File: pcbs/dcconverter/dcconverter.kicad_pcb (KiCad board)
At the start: 2 copper layers, 149.9 x 149.9 mm, 41 parts, among them IC1 NCP7805TG, J1 190-9991, J2 766-6629, J3 146-8335, J4 766-6604, J5 766-6604, Q1 NGTB40N120FL2WG, Q10 398-433, Q2 FQP47P06, Q3 2SK3747-1E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

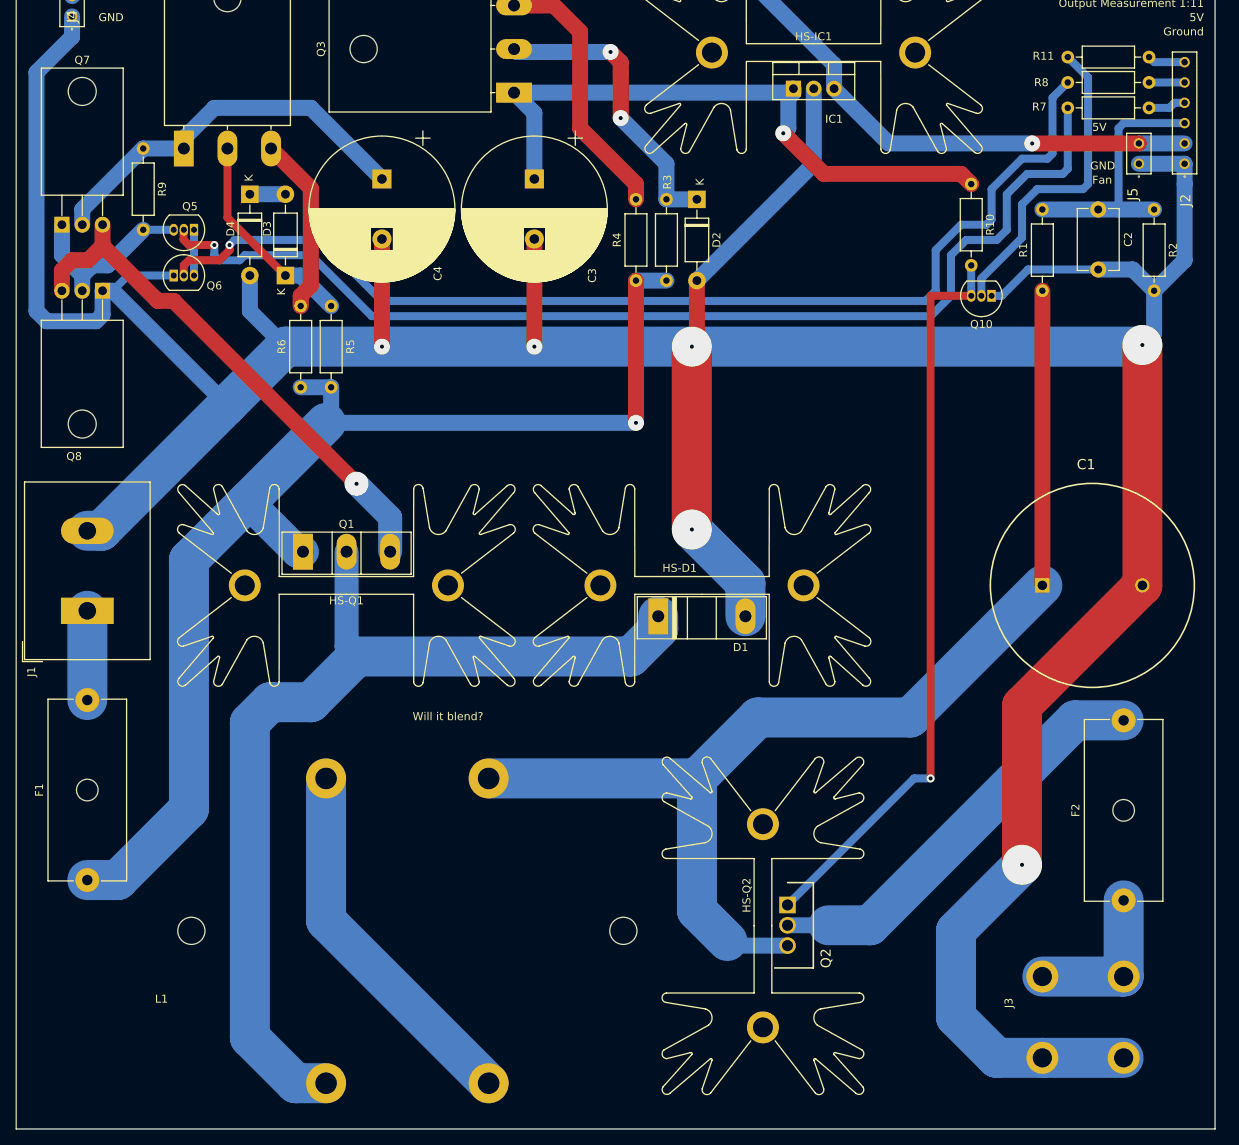
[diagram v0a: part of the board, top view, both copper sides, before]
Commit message: Make Tracks with a high Current as thick as possible
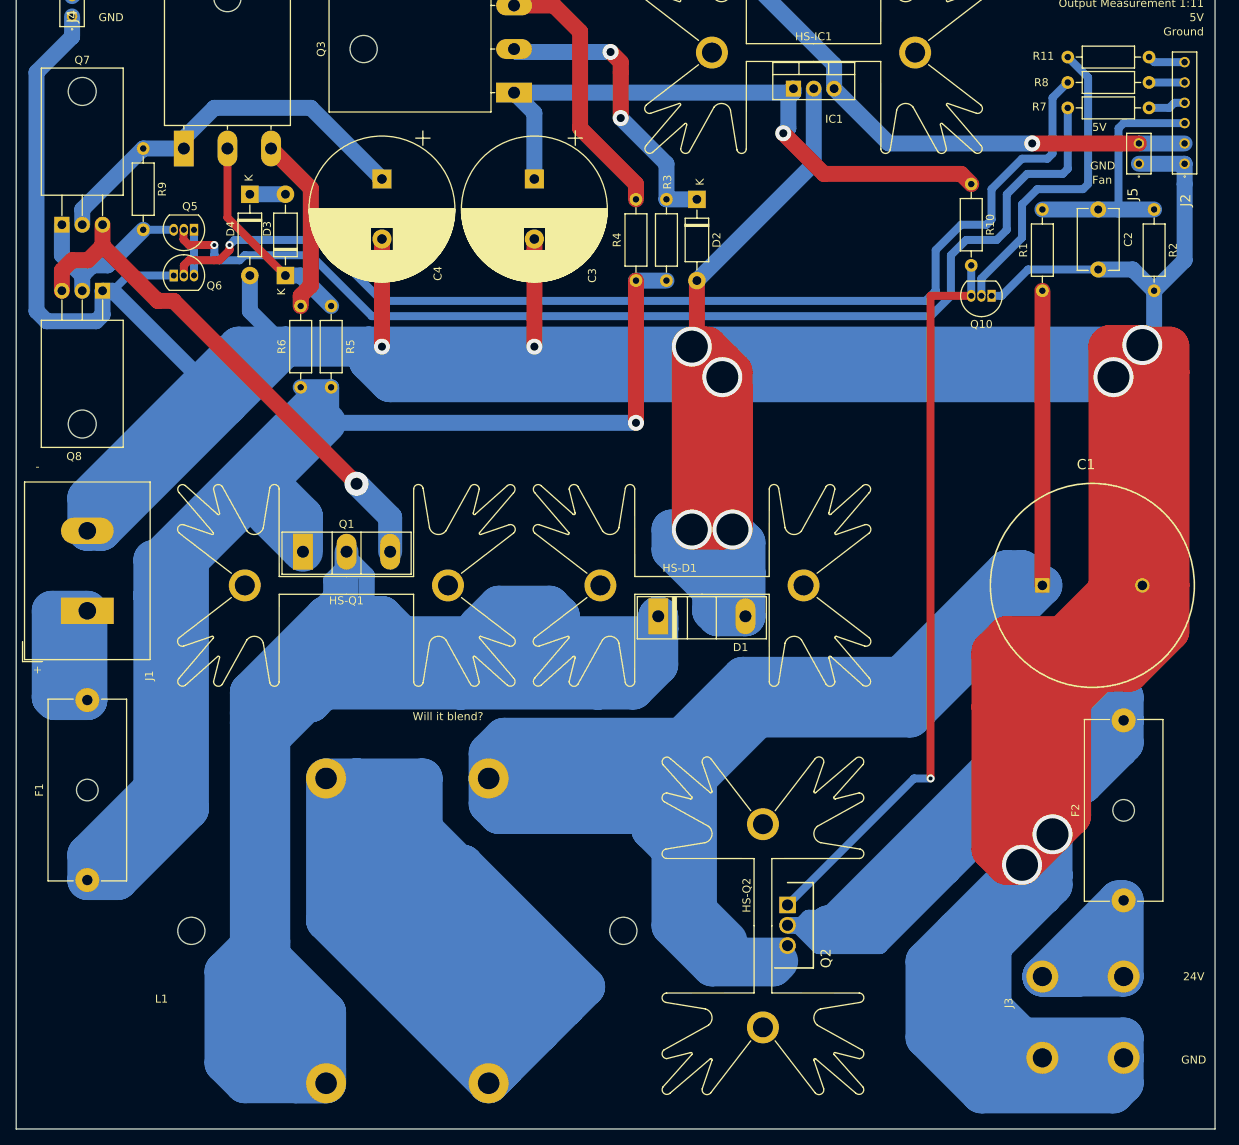
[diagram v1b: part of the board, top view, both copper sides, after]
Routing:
- net Net-(C1-Pad2): track 505.8 -> 1087.3 mm, vias 6 -> 10
- net Net-(D1-Pad1): track 122.4 -> 421.2 mm
- net Net-(C1-Pad1): track 145.7 -> 365.8 mm
- net Net-(L1-Pad2): track 46.5 -> 234.7 mm
- net Net-(F2-Pad2): track 52.6 -> 199.9 mm
- net Net-(F1-Pad1): track 149.8 -> 238.6 mm
- net Net-(F1-Pad2): track 11.2 -> 35.6 mm
- net Net-(F2-Pad1): track 19.7 -> 41.8 mm
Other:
- board text added: "+"
- board text added: "-"
- board text added: "24V"

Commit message: Empty PCB
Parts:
- removed C1: 845-4749, SamacSys_Parts:CAPPRD1250W100D2550H5200
- removed C2: 831-2929, Capacitor_THT:C_Disc_D7.5mm_W5.0mm_P7.50mm
- removed C3, C4: 711-2096, Capacitor_THT:CP_Radial_D18.0mm_P7.50mm
- removed D1: 192-966, Diode_THT:D_DO-247_Vertical
- removed D2: 805-0094, Diode_THT:D_DO-41_SOD81_P10.16mm_Horizontal
- removed D3, D4: 800-8872, Diode_THT:D_DO-41_SOD81_P10.16mm_Horizontal
- removed F1, F2: 176-9047, Fuse:Fuseholder_Cylinder-5x20mm_Schurter_0031_8201_Horizontal_Open
- removed HS-D1, HS-IC1, HS-Q1, HS-Q2: 893-4942, Heatsink:Heatsink_Fischer_SK129-STS_42x25mm_2xDrill2.5mm
- removed IC1: NCP7805TG, Package_TO_SOT_THT:TO-220-3_Vertical
- removed J1: 190-9991, TerminalBlock_Dinkle:TerminalBlock_Dinkle_DT-55-B01X-02_P10.00mm
- removed J2: 766-6629, SamacSys_Parts:CES-106-XX-Y-S
- removed J3: 146-8335, dcconverter:connector_2pin_P10.6mm
- removed J4, J5: 766-6604, SamacSys_Parts:CES-102-XX-Y-S
- removed L1: 769-0587, dcconverter:rb8522_size5
- removed Q1: NGTB40N120FL2WG, Package_TO_SOT_THT:TO-247-3_Vertical
- removed Q10, Q5, Q6: 398-433, Package_TO_SOT_THT:TO-92_Inline
- removed Q2: FQP47P06, TO254P483X1016X2261-3P
- removed Q3, Q4: 2SK3747-1E, Package_TO_SOT_THT:TO-3P-3_Horizontal_TabDown
- removed Q7: 671-5118, Package_TO_SOT_THT:TO-220-3_Horizontal_TabDown
- removed Q8: 671-4809, Package_TO_SOT_THT:TO-220-3_Horizontal_TabDown
- removed R1: 1M, Resistor_THT:R_Axial_DIN0207_L6.3mm_D2.5mm_P10.16mm_Horizontal
- removed R10: 10k, Resistor_THT:R_Axial_DIN0207_L6.3mm_D2.5mm_P10.16mm_Horizontal
- removed R11, R7, R8: 220, Resistor_THT:R_Axial_DIN0207_L6.3mm_D2.5mm_P10.16mm_Horizontal
- removed R2: 100k, Resistor_THT:R_Axial_DIN0207_L6.3mm_D2.5mm_P10.16mm_Horizontal
- removed R3, R5: 10M, Resistor_THT:R_Axial_DIN0207_L6.3mm_D2.5mm_P10.16mm_Horizontal
- removed R4, R6: 707-8546, Resistor_THT:R_Axial_DIN0207_L6.3mm_D2.5mm_P10.16mm_Horizontal
- removed R9: 1k, Resistor_THT:R_Axial_DIN0207_L6.3mm_D2.5mm_P10.16mm_Horizontal
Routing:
- net Net-(C1-Pad2): track 1087.3 -> 0.00 mm, vias 10 -> 0
- net Net-(D1-Pad1): track 421.2 -> 0.00 mm
- net Net-(C1-Pad1): track 365.8 -> 0.00 mm
- net Net-(F1-Pad1): track 238.6 -> 0.00 mm, vias 1 -> 0
- net Net-(L1-Pad2): track 234.7 -> 0.00 mm
- net Net-(F2-Pad2): track 199.9 -> 0.00 mm
- net Net-(IC1-Pad3): track 152.1 -> 0.00 mm, vias 1 -> 0
- net Net-(Q5-Pad2): track 137.8 -> 0.00 mm, vias 1 -> 0
- net Net-(Q6-Pad2): track 137.2 -> 0.00 mm, vias 1 -> 0
- net Net-(Q10-Pad3): track 93.7 -> 0.00 mm, vias 1 -> 0
- net Net-(C3-Pad1): track 79.2 -> 0.00 mm, vias 1 -> 0
- net Net-(Q1-Pad3): track 65.8 -> 0.00 mm, vias 1 -> 0
- net Net-(C4-Pad1): track 49.1 -> 0.00 mm
- net Net-(F2-Pad1): track 41.8 -> 0.00 mm
- net Net-(Q10-Pad2): track 39.8 -> 0.00 mm
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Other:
- board outline removed
- board text removed: "+"
- board text removed: "-"
- board text removed: "24V"
- board text removed: "5V"
- board text removed: "Controller Connection Pins"
- board text removed: "Fan"
- board text removed: "GND"
- board text removed: "Ground"
- board text removed: "IGBT Control Signal (5V)"
- board text removed: "IGBT ON/OFF (5V)"
- board text removed: "Output Measurement 1:11"
- board text removed: "Output ON/OFF (5V)"
- board text removed: "Will it blend?"

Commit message: Fix Heatsinks
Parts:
- added C1: 10mF, Custom:CAPPRD1250W100D2550H5200, F.Cu at (121.9, 115.6)
- added C2: 10nF, Capacitor_THT:C_Disc_D14.5mm_W5.0mm_P7.50mm, F.Cu at (174.3, 76.1)
- added C3: 1uF, Capacitor_THT:CP_Radial_D8.0mm_P2.50mm, F.Cu at (162.4, 118.7)
- added C4: 10nF, Capacitor_THT:C_Disc_D14.5mm_W5.0mm_P7.50mm, F.Cu at (157.3, 98.5)
- added C5: 1uF, Capacitor_THT:CP_Radial_D8.0mm_P2.50mm, F.Cu at (172.8, 104.4)
- added D1: DSS60-0045B, Custom:DSS60-0045B_Vertical, F.Cu at (110.8, 132.0)
- added D2: 1N4751ATR, Diode_THT:D_DO-41_SOD81_P10.16mm_Horizontal, F.Cu at (95.5, 104.3)
- added D3: 1N5956BRLG, Diode_THT:D_DO-41_SOD81_P10.16mm_Horizontal, F.Cu at (121.8, 83.6)
- added D4: 1N5956BRLG, Diode_THT:D_DO-41_SOD81_P10.16mm_Horizontal, F.Cu at (77.6, 133.4)
- added D5: 1N5408G, Custom:1N5408G, F.Cu at (104.1, 84.1)
- added F1: 2A, Fuse:Fuseholder_Cylinder-5x20mm_Schurter_0031_8201_Horizontal_Open, F.Cu at (181.4, 45.3)
- added F2: 25A, Fuse:Fuseholder_Cylinder-5x20mm_Schurter_0031_8201_Horizontal_Open, F.Cu at (82.8, 125.7)
- added HS-D1: HeatsinkUpright, Custom:HeatsinkUpright, F.Cu at (120.5, 47.3)
- added HS-IC1: HeatsinkUpright, Custom:HeatsinkUpright, F.Cu at (61.0, 114.3)
- added HS-Q1: HeatsinkUpright, Custom:HeatsinkUpright, F.Cu at (113.2, 94.7)
- added HS-Q2: HeatsinkUpright, Custom:HeatsinkUpright, F.Cu at (159.6, 47.3)
- added IC1: NCP7805TG, Package_TO_SOT_THT:TO-220-3_Vertical, F.Cu at (141.6, 132.8)
- added J1: 190-9991, Custom:TerminalBlock_2pin_10mm, F.Cu at (150.1, 115.2)
- added J2: Conn_01x01, Custom:SLB4-I90, F.Cu at (101.6, 67.4)
- added J3: Conn_01x01, Custom:SLB4-I90, F.Cu at (42.1, 134.5)
- added J4: 146-8335, Custom:connector_2pin_P10.6mm, F.Cu at (196.5, 68.0)
- added J5: Conn_01x01, Custom:SLB4-I90, F.Cu at (81.3, 119.3)
- added J6: Conn_01x01, Custom:SLB4-I90, F.Cu at (101.6, 80.7)
- added J7: 483-8461, Custom:Molex_KK_254_2pin, F.Cu at (206.9, 46.1)
- added J8: 483-8461, Custom:Molex_KK_254_2pin, F.Cu at (108.3, 126.5)
- added L1: RB8522-25-2M0, Custom:rb8522_size5, F.Cu at (71.1, 63.4)
- added Q1: NGTB40N120FL2WG, Custom:NGTB40N120FL2WG_Vertical, F.Cu at (156.3, 91.8)
- added Q10: TS13003CT, Custom:TS13003CT_wide, F.Cu at (171.5, 58.1)
- added Q2: FQP47P06, Custom:FQP47P06_Vertical_Wide, F.Cu at (195.6, 75.0)
- added Q3: 2SK3747-1E, Custom:2SK3747_TabDown, F.Cu at (155.8, 82.6)
- added Q4: 2SK3747-1E, Custom:2SK3747_TabDown, F.Cu at (138.4, 82.6)
- added Q5: TS13003CT, Custom:TS13003CT_wide, F.Cu at (171.5, 69.7)
- added Q6: TS13003CT, Custom:TS13003CT_wide, F.Cu at (171.5, 63.9)
- added Q7: FQP3P50, Custom:FQP3P50_Horizontal_TabDown, F.Cu at (144.8, 108.9)
- added Q8: FDP20N50, Custom:FDP20N50_Horizontal_TabDown, F.Cu at (182.4, 71.1)
- added R1: 1MOhm, Resistor_THT:R_Axial_DIN0207_L6.3mm_D2.5mm_P10.16mm_Horizontal, F.Cu at (171.6, 81.4)
- added R10: 10kOhm, Resistor_THT:R_Axial_DIN0207_L6.3mm_D2.5mm_P10.16mm_Horizontal, F.Cu at (184.9, 81.4)
- added R11: 220, Resistor_THT:R_Axial_DIN0207_L6.3mm_D2.5mm_P10.16mm_Horizontal, F.Cu at (160.2, 111.9)
- added R12: 10kOhm, Resistor_THT:R_Axial_DIN0207_L6.3mm_D2.5mm_P10.16mm_Horizontal, F.Cu at (184.9, 85.5)
- added R13: 10MOhm, Resistor_THT:R_Axial_DIN0207_L6.3mm_D2.5mm_P10.16mm_Horizontal, F.Cu at (91.2, 133.3)
- added R2: 100kOhm, Resistor_THT:R_Axial_DIN0207_L6.3mm_D2.5mm_P10.16mm_Horizontal, F.Cu at (171.6, 85.5)
- added R3: 10MOhm, Resistor_THT:R_Axial_DIN0207_L6.3mm_D2.5mm_P10.16mm_Horizontal, F.Cu at (170.7, 97.6)
- added R4: 1MOhm, Resistor_THT:R_Axial_DIN0207_L6.3mm_D2.5mm_P10.16mm_Horizontal, F.Cu at (154.6, 103.8)
- added R5: 10MOhm, Resistor_THT:R_Axial_DIN0207_L6.3mm_D2.5mm_P10.16mm_Horizontal, F.Cu at (143.1, 121.8)
- added R6: 1MOhm, Resistor_THT:R_Axial_DIN0207_L6.3mm_D2.5mm_P10.16mm_Horizontal, F.Cu at (154.6, 107.9)
- added R7: 220Ohm, Resistor_THT:R_Axial_DIN0207_L6.3mm_D2.5mm_P10.16mm_Horizontal, F.Cu at (126.6, 130.9)
- added R8: 220Ohm, Resistor_THT:R_Axial_DIN0207_L6.3mm_D2.5mm_P10.16mm_Horizontal, F.Cu at (172.1, 89.5)
- added R9: 1MOhm, Resistor_THT:R_Axial_DIN0207_L6.3mm_D2.5mm_P10.16mm_Horizontal, F.Cu at (172.1, 93.6)
- added XA1: Arduino_Micro_Socket, Custom:Arduino_Micro_Socket, F.Cu at (44.3, 106.0)

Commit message: Place PCB
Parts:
- moved R8 155.6 mm to (17.1, 74.9)
- moved Q6 152.5 mm to (19.1, 65.4), turned to 270 degrees
- moved Q8 150.7 mm to (31.8, 66.0)
- moved Q5 146.1 mm to (25.4, 70.5), turned to 90 degrees
- moved J1 145.0 mm to (18.4, 54.6), turned to 270 degrees
- moved R12 133.6 mm to (63.4, 29.8), turned to 180 degrees
- moved R9 133.5 mm to (40.6, 70.5), turned to 180 degrees
- moved R11 128.3 mm to (34.9, 84.5), turned to 180 degrees
- moved R3 126.8 mm to (45.1, 80.0), turned to 90 degrees
- moved C5 120.7 mm to (59.1, 64.1), turned to 90 degrees
- moved C2 119.2 mm to (55.2, 81.9)
- moved R6 116.5 mm to (56.5, 45.1), turned to 270 degrees
- moved C3 111.9 mm to (59.7, 74.3), turned to 90 degrees
- moved R7 111.2 mm to (30.5, 74.9)
- moved F1 110.3 mm to (73.7, 21.6), turned to 180 degrees
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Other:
- copper layers 2 -> 4

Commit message: Improve Placement
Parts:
- added REF**: MountingHole_5mm_Pad, MountingHole:MountingHole_5mm_Pad, F.Cu at (168.5, 108.5)
- added REF**: MountingHole_5mm_Pad, MountingHole:MountingHole_5mm_Pad, F.Cu at (21.5, 108.5)
- added REF**: MountingHole_5mm_Pad, MountingHole:MountingHole_5mm_Pad, F.Cu at (21.5, 21.5)
- moved Q10 158.9 mm to (-43.2, 22.9)
- moved R10 158.9 mm to (-48.3, 17.1)
- moved J7 96.3 mm to (154.0, 111.0), turned to 0 degrees
- moved R1 91.2 mm to (108.5, 98.0), turned to 0 degrees
- moved R2 86.8 mm to (107.5, 105.5), turned to 0 degrees
- moved R6 84.8 mm to (38.5, 128.0), turned to 180 degrees
- moved R7 72.3 mm to (79.0, 128.5)
- moved J8 65.3 mm to (55.5, 28.0), turned to 180 degrees
- moved D2 60.3 mm to (81.5, 121.0), turned to 0 degrees
- moved R11 56.3 mm to (68.0, 130.0)
- moved J4 54.6 mm to (139.5, 95.0), turned to 180 degrees
- moved C4 54.1 mm to (89.0, 101.0), turned to 180 degrees
- moved F2 45.7 mm to (171.0, 95.5)
- moved C2 44.0 mm to (89.5, 109.5), turned to 180 degrees
- moved Q3 32.7 mm to (52.0, 63.0), turned to 0 degrees
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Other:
- board outline added: 160 x 100 mm

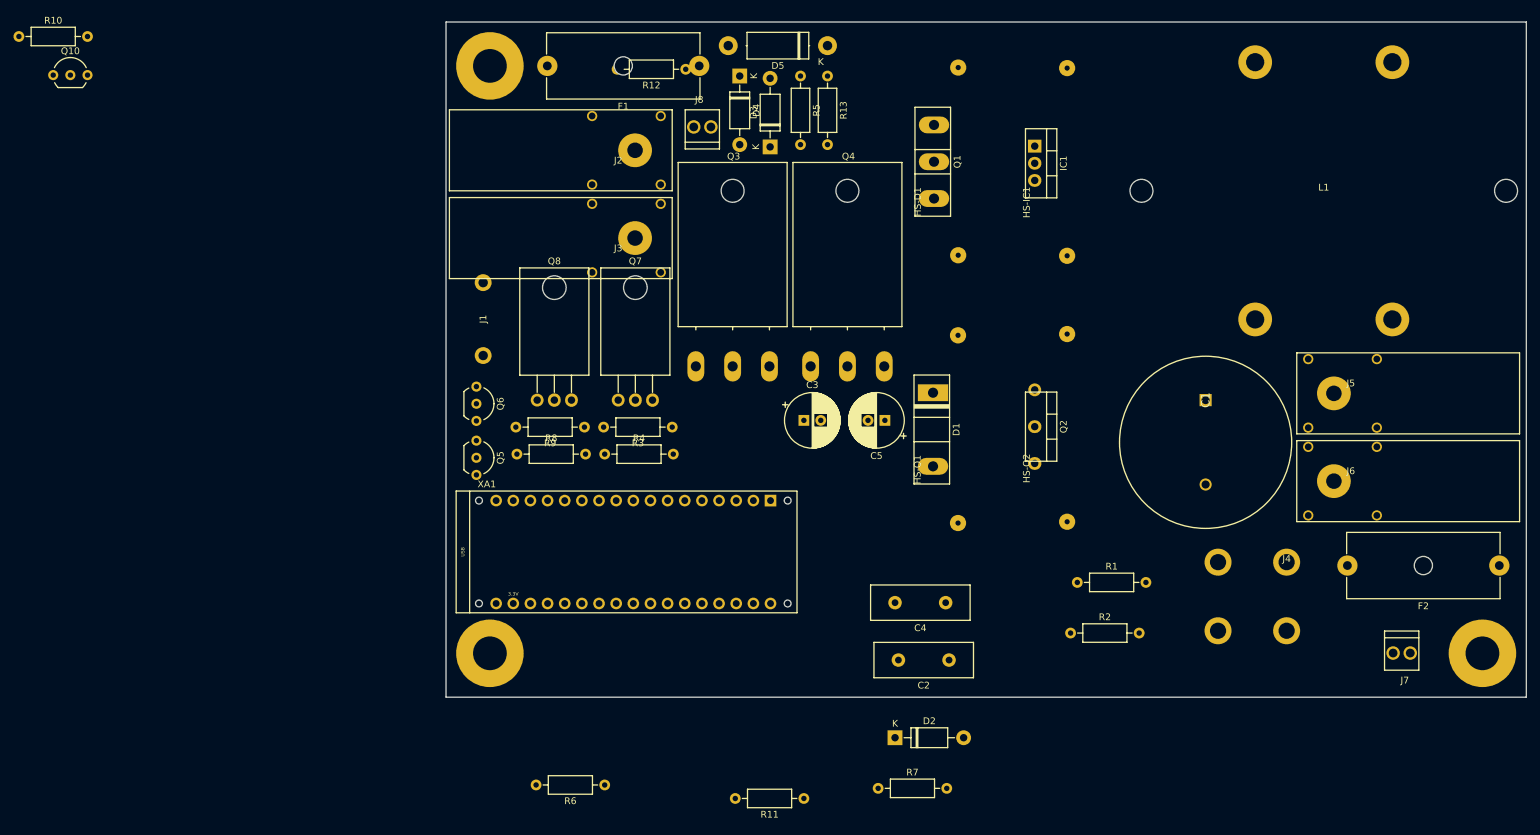
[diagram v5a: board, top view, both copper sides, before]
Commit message: Start routing PCB
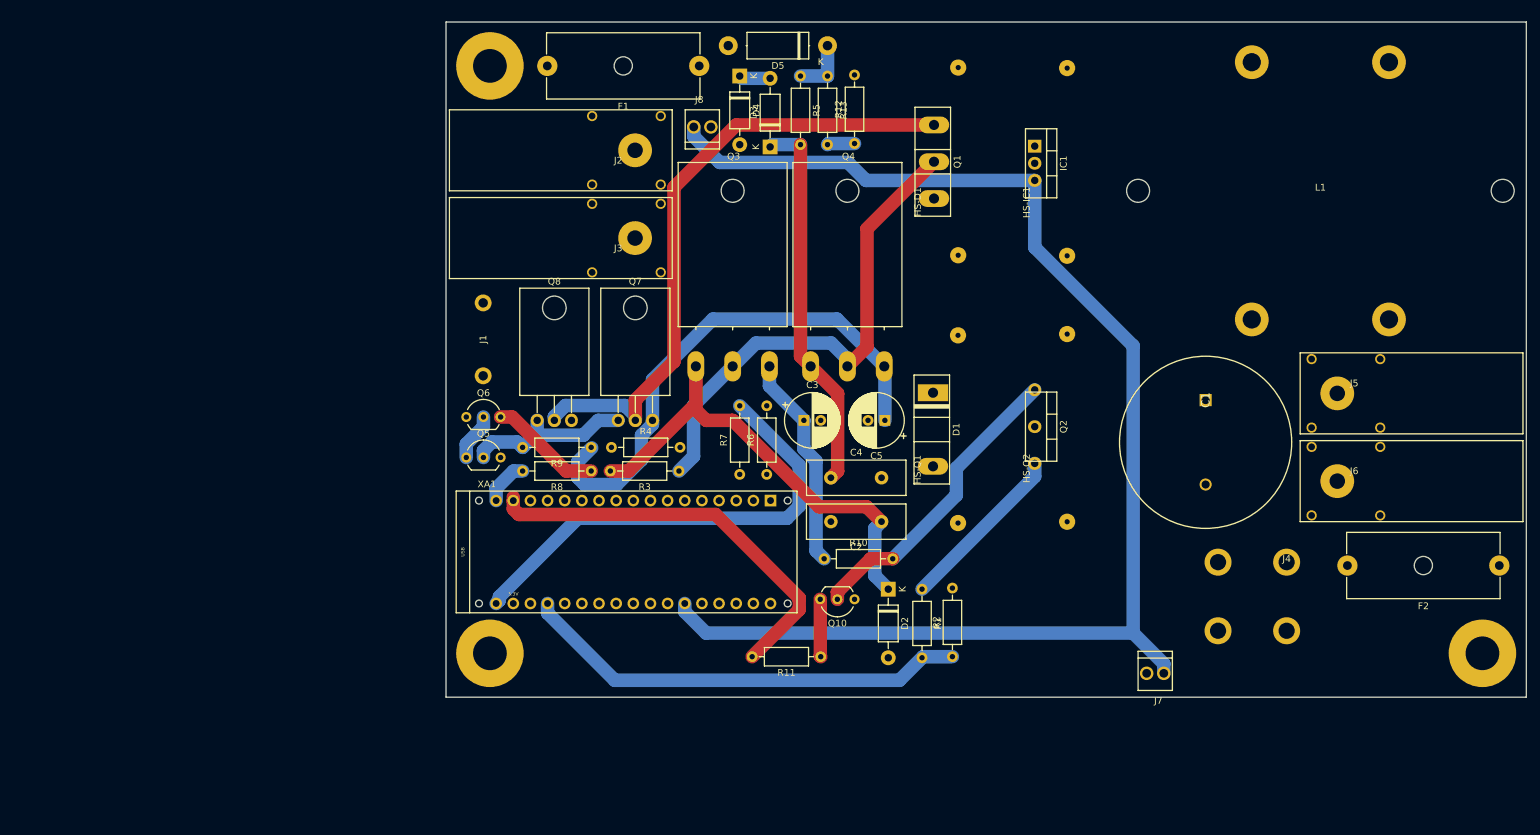
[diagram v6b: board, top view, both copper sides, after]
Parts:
- moved R10 142.2 mm to (71.0, 94.5)
- moved Q10 141.8 mm to (75.5, 100.5), turned to 180 degrees
- moved R6 51.9 mm to (62.5, 82.0), turned to 90 degrees
- moved R7 50.8 mm to (58.5, 82.0), turned to 90 degrees
- moved J7 36.6 mm to (117.5, 114.0)
- moved R12 27.3 mm to (75.5, 33.0), turned to 90 degrees
- moved C4 25.1 mm to (72.0, 82.5), turned to 0 degrees
- moved R1 23.0 mm to (85.5, 99.0), turned to 270 degrees
- moved C2 22.8 mm to (79.5, 89.0)
- moved D2 22.0 mm to (80.5, 99.0), turned to 270 degrees
- moved R11 21.1 mm to (70.5, 109.0)
- moved R2 17.8 mm to (90.0, 109.0), turned to 90 degrees
- moved R8 11.3 mm to (36.5, 81.5), turned to 180 degrees
- moved R3 6.58 mm to (49.5, 81.5)
- moved Q6 4.74 mm to (18.0, 73.5), turned to 0 degrees
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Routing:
- net Net-(C1-Pad2): track 0.00 -> 430.7 mm
- net Net-(IC1-Pad3): track 0.00 -> 204.5 mm
- net Net-(R12-Pad1): track 0.00 -> 126.5 mm
- net Net-(D5-Pad1): track 0.00 -> 113.0 mm
- net Net-(D1-Pad1): track 0.00 -> 110.3 mm
- net Net-(Q1-Pad3): track 0.00 -> 93.7 mm
- net Net-(F2-Pad2): track 0.00 -> 91.9 mm
- net Net-(C1-Pad1): track 0.00 -> 91.0 mm
- net Net-(F2-Pad1): track 0.00 -> 89.0 mm
- net Net-(C5-Pad1): track 0.00 -> 78.2 mm
- net Net-(R7-Pad2): track 0.00 -> 69.7 mm
- net Net-(C2-Pad1): track 0.00 -> 68.8 mm
- net Net-(R1-Pad2): track 0.00 -> 67.0 mm
- net Net-(C2-Pad2): track 0.00 -> 62.9 mm
- net Net-(R11-Pad2): track 0.00 -> 61.1 mm
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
